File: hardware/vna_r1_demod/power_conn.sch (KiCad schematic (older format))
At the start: 40 parts, among them J401 Conn_02x05_Odd_Even, U401 ADP7158, U402 74HC244, U403 LD39100

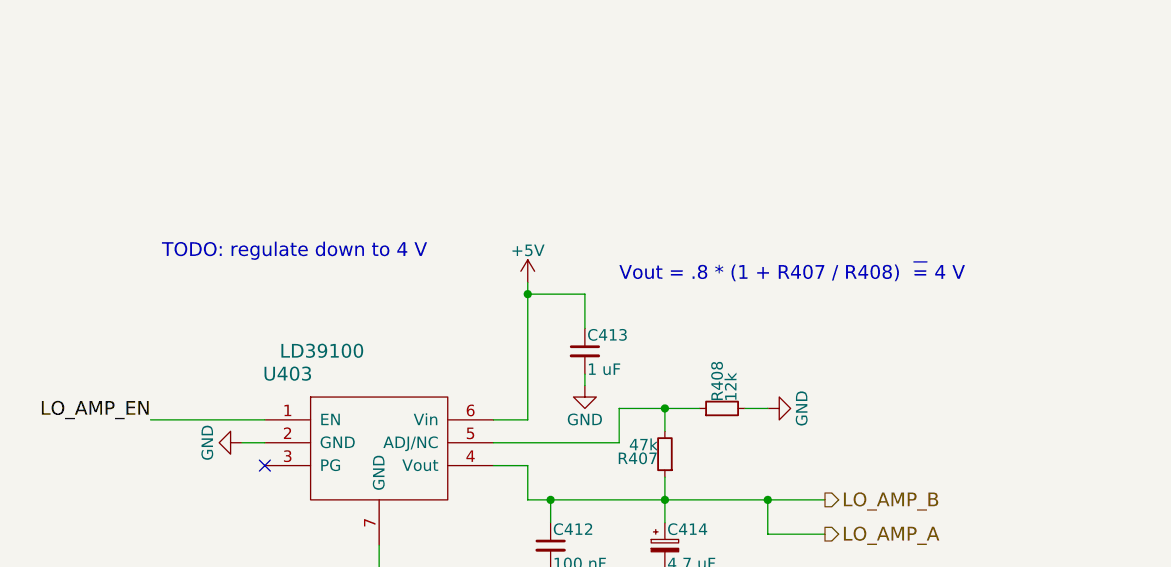
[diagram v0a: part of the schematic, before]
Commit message: fix MAAM-011100 bias voltage divider and LD39100PUR regulator adjust circuit on vna_r1_synth. thanks Santiago!
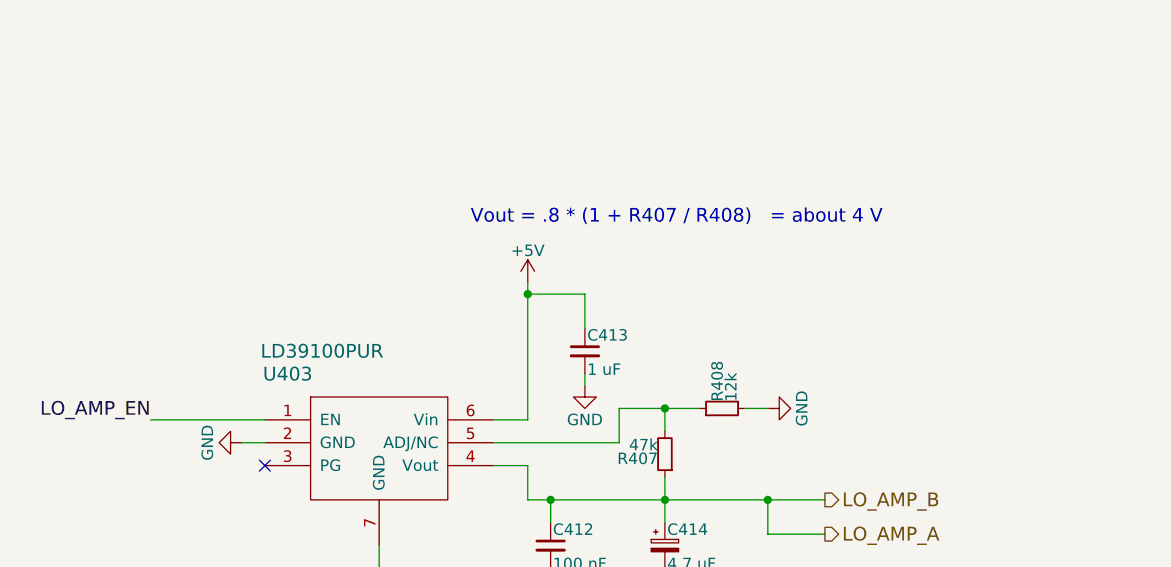
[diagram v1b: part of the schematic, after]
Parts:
- U403: value LD39100 -> LD39100PUR
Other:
- note added: "Vout = .8 * (1 + R407 / R408) = about 4 V"
- note removed: "TODO: regulate down to 4 V"
- note removed: "Vout = .8 * (1 + R407 / R408) ~= 4 V"
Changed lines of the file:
@@
 	1    0    0    -1
 $EndComp
-Text Notes 7600 2200 0    60   ~ 0
-TODO: regulate down to 4 V
 $Comp
 L GND #PWR073
@@
 P 8550 3000
 F 0 "U403" H 8150 3300 60  0000 C CNN
-F 1 "LD39100" H 8300 3400 60  0000 C CNN
+F 1 "LD39100PUR" H 8300 3400 60  0000 C CNN
 F 2 "Housings_DFN_QFN:DFN-6-1EP_3x3mm_Pitch0.95mm" H 8550 3000 60  0001 C CNN
 F 3 "" H 8550 3000 60  0001 C CNN
@@
 Wire Wire Line
 	7550 2900 8050 2900
-Text Notes 9600 2300 0    60   ~ 0
-Vout = .8 * (1 + R407 / R408)  ~= 4 V
+Text Notes 8950 2050 0    60   ~ 0
+Vout = .8 * (1 + R407 / R408)   = about 4 V
 $Comp
 L R_Small R407

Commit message: bypass if filter in vna r1 demod
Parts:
- C401, C402, C403, C404, C405, C406, C407, C408, C409, C412, C413: symbol C_Small -> device:C_Small
- C410, C411, C414: symbol CP_Small -> device:CP_Small
- D401: symbol LED -> vna_r1_demod-rescue:LED
- F401: symbol Polyfuse_Small -> vna_r1_demod-rescue:Polyfuse_Small
- H401, H402, H403, H404, H405, H406, H407, H408, H409: symbol MOUNTING_HOLE -> mounting_hole:MOUNTING_HOLE
- J401: symbol Conn_02x05_Odd_Even -> vna_r1_demod-rescue:Conn_02x05_Odd_Even
- L401, L402: symbol L_Small -> device:L_Small
- R401, R402, R403, R404, R405, R406, R407, R408, R409: symbol R_Small -> device:R_Small
- U401: symbol ADP7158 -> adp7158:ADP7158
- U402: symbol 74HC244 -> vna_r1_demod-rescue:74HC244
- U403: symbol LD39100 -> ld39100:LD39100
